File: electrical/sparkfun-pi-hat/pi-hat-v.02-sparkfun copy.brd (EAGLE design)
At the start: 86.4 x 53.3 mm, 13 parts, among them J1 PIN20X2

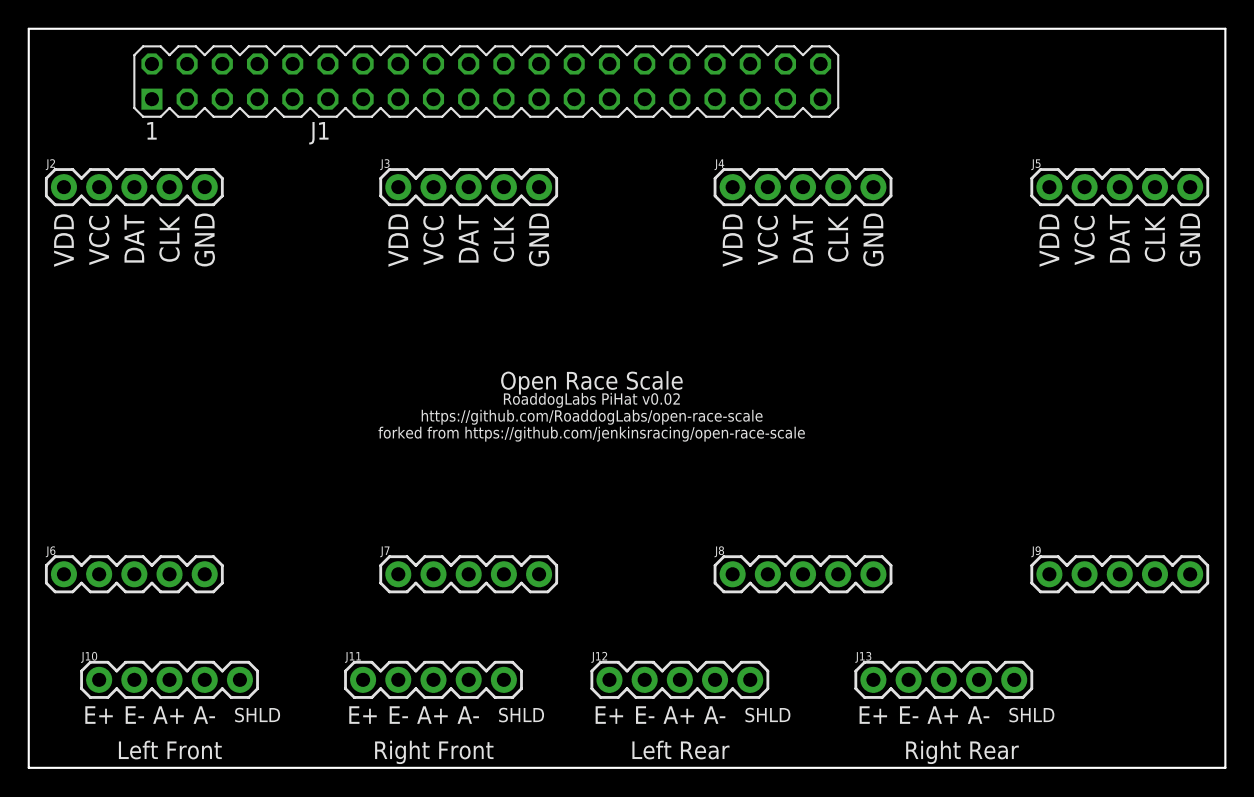
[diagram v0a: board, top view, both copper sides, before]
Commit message: update schematic and board, generate gerbers
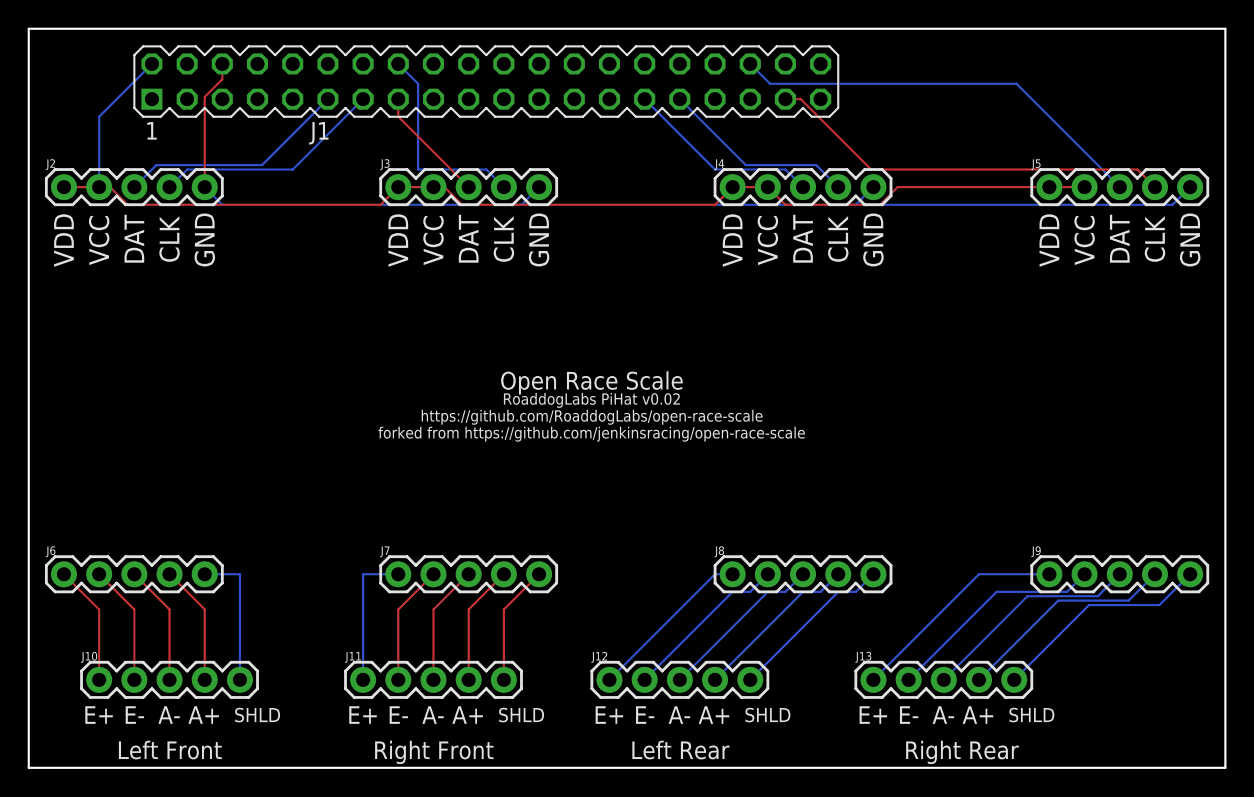
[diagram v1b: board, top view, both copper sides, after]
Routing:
- net N$17: track 0.00 -> 87.3 mm
- net N$18: track 0.00 -> 85.2 mm
- net N$24: track 0.00 -> 30.4 mm
- net N$23: track 0.00 -> 29.3 mm
- net N$20: track 0.00 -> 16.6 mm
- net N$19: track 0.00 -> 16.6 mm
- net N$29: track 0.00 -> 15.9 mm
- net N$28: track 0.00 -> 15.9 mm
- net N$27: track 0.00 -> 15.9 mm
- net N$16: track 0.00 -> 15.9 mm
- net N$30: track 0.00 -> 15.9 mm
- net N$22: track 0.00 -> 14.9 mm
- net N$26: track 0.00 -> 14.1 mm
- net N$25: track 0.00 -> 14.1 mm
- net N$13: track 0.00 -> 12.0 mm
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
